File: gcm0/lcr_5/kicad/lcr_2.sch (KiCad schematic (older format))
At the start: 125 parts, among them J1 5V, J2 -5V, J3 Conn_01x01_Male, J7 sin, Q1 BC547, Q2 BC547, Q3 BC547, SW1 1, SW2 2, SW3 SW_DIP_x01, U1 RC4580, U10 RC4580, U11 74HC595, U12 STM32F030F4P6, U13 L7809, U2 74HC4053PW,112, U3 74HC4052PW,118, U4 RC4580, U5 LM2596S-5, U6 LM7805_TO220, U7 RC4580, U8 LM1117-3.3, U9 74HC4053PW,112, Y1 8M

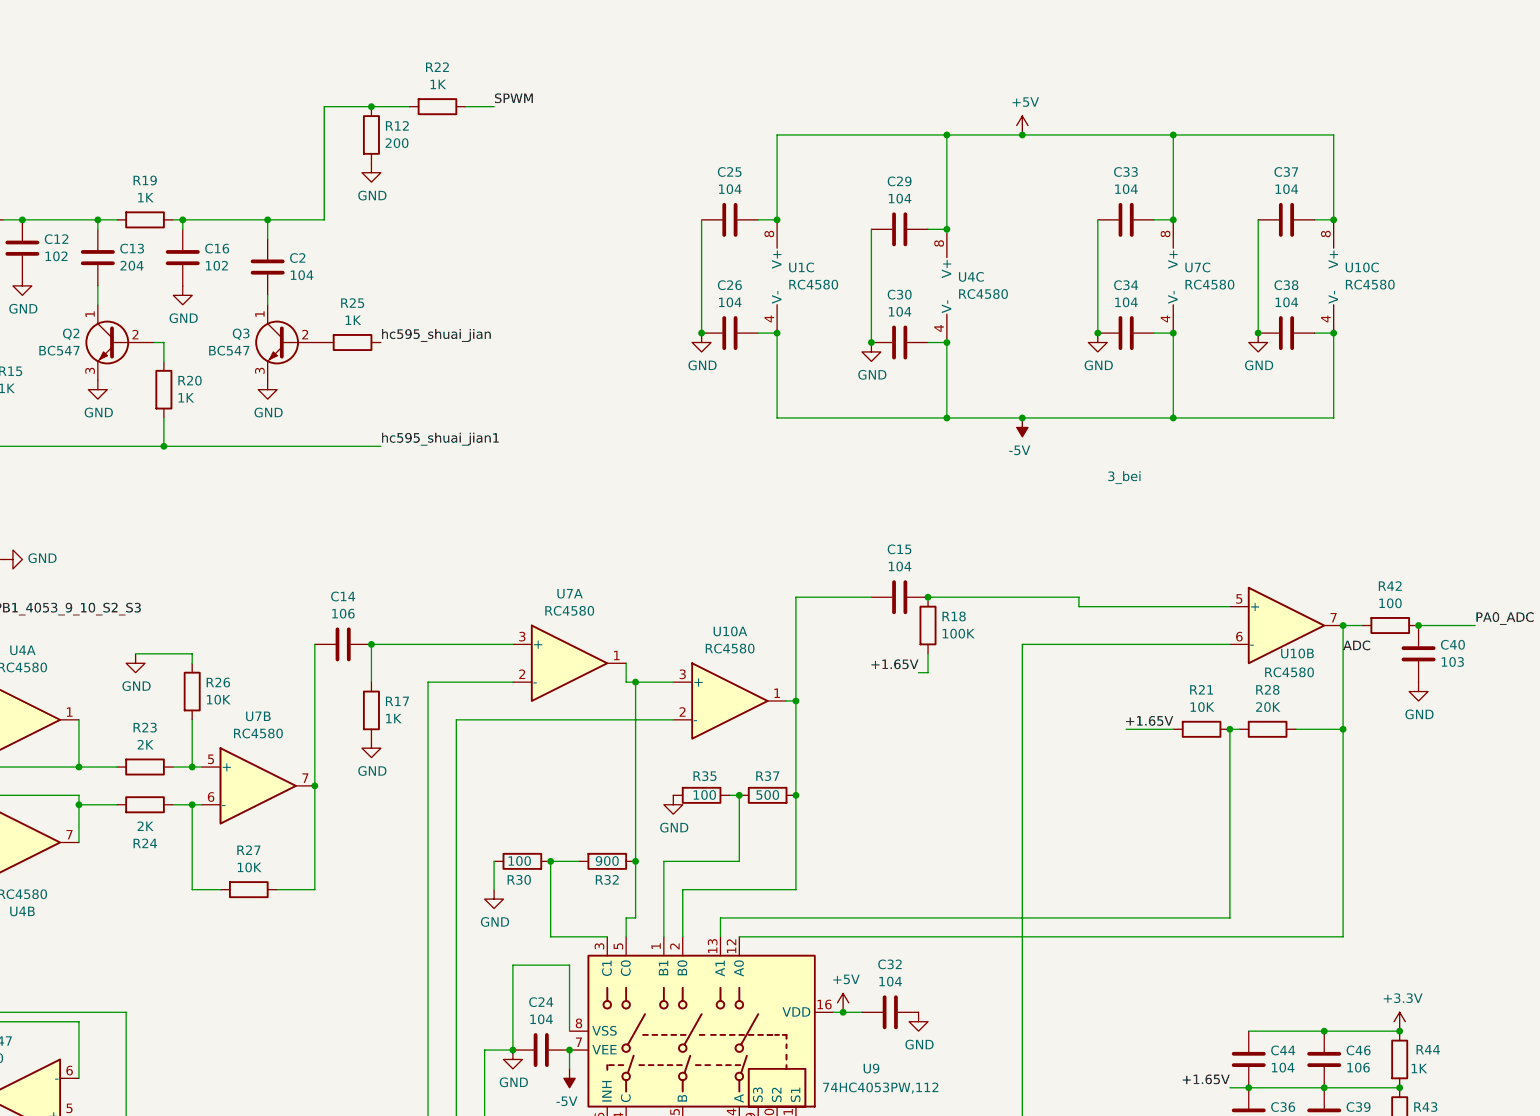
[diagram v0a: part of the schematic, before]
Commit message: 修改采样率
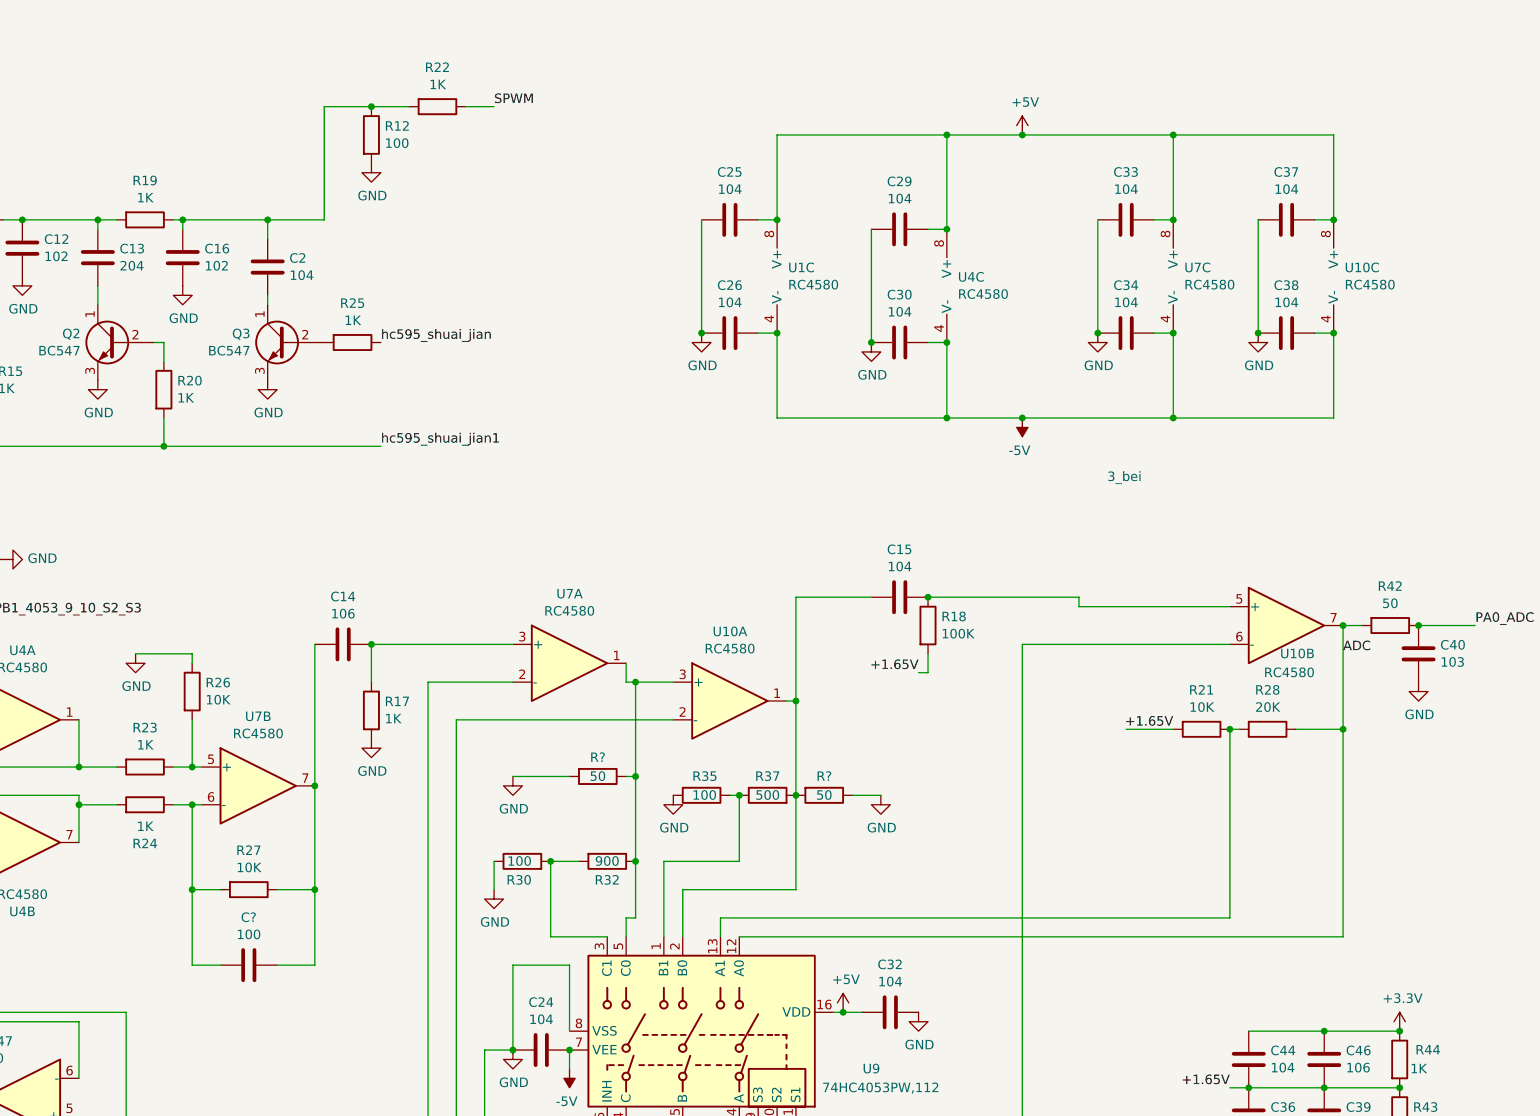
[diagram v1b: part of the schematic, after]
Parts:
- added C?: 100, symbol Device:C
- added R? (x2): 50, symbol Device:R
- R12: value 200 -> 100
- R23, R24: value 2K -> 1K
- R42: value 100 -> 50
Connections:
- net GND: now also R?.1, R?.2
- net at R32.1, U10.3 (+), U7.1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: now also R?.1
- net at R24.1, R27.2, U7.6 (-): now also C?.2
- net at C14.2, R27.1, U7.7: now also C?.1
- net at C15.2, R37.2, U10.1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: now also R?.2
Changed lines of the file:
@@
 P 4350 4450
 F 0 "R23" V 4143 4450 50  0000 C CNN
-F 1 "2K" V 4234 4450 50  0000 C CNN
+F 1 "1K" V 4234 4450 50  0000 C CNN
 F 2 "Resistor_THT:R_Axial_DIN0204_L3.6mm_D1.6mm_P1.90mm_Vertical" V 4280 4450 50  0001 C CNN
 F 3 "~" H 4350 4450 50  0001 C CNN
@@
 P 4350 4650
 F 0 "R24" V 4143 4650 50  0000 C CNN
-F 1 "2K" V 4234 4650 50  0000 C CNN
+F 1 "1K" V 4234 4650 50  0000 C CNN
 F 2 "Resistor_THT:R_Axial_DIN0204_L3.6mm_D1.6mm_P1.90mm_Vertical" V 4280 4650 50  0001 C CNN
 F 3 "~" H 4350 4650 50  0001 C CNN
@@
 P 10950 3700
 F 0 "R42" V 10743 3700 50  0000 C CNN
-F 1 "100" V 10834 3700 50  0000 C CNN
+F 1 "50" V 10834 3700 50  0000 C CNN
 F 2 "Resistor_THT:R_Axial_DIN0204_L3.6mm_D1.6mm_P1.90mm_Vertical" V 10880 3700 50  0001 C CNN
 F 3 "~" H 10950 3700 50  0001 C CNN
@@
 3_bei
 Wire Wire Line
-	6950 4000 6950 4950
+	6950 4000 6950 4500
 Wire Wire Line
 	6900 5250 6950 5250
@@
 P 5550 1100
 F 0 "R12" H 5620 1146 50  0000 L CNN
-F 1 "200" H 5620 1055 50  0000 L CNN
+F 1 "100" H 5620 1055 50  0000 L CNN
 F 2 "Resistor_THT:R_Axial_DIN0204_L3.6mm_D1.6mm_P1.90mm_Vertical" V 5480 1100 50  0001 C CNN
 F 3 "~" H 5550 1100 50  0001 C CNN
@@
 Connection ~ 10600 5850
 Connection ~ 11000 5850
+$Comp
+L Device:C C?
+U 1 1 62123A2D
+P 4900 5500
+F 0 "C?" V 4648 5500 50  0000 C CNN
+F 1 "100" V 4739 5500 50  0000 C CNN
+F 2 "" H 4938 5350 50  0001 C CNN
+F 3 "~" H 4900 5500 50  0001 C CNN
+	1    4900 5500
+	0    1    1    0
+$EndComp
+Wire Wire Line
+	5050 5500 5250 5500
+Wire Wire Line
+	5250 5500 5250 5100
+Connection ~ 5250 5100
+Wire Wire Line
+	4750 5500 4600 5500
+Wire Wire Line
+	4600 5500 4600 5100
+Connection ~ 4600 5100
+$Comp
+L Device:R R?
+U 1 1 621AA26F
+P 6750 4500
+F 0 "R?" V 6650 4500 50  0000 C CNN
+F 1 "50" V 6750 4500 50  0000 C CNN
+F 2 "" V 6680 4500 50  0001 C CNN
+F 3 "~" H 6750 4500 50  0001 C CNN
+	1    6750 4500
+	0    1    1    0
+$EndComp
+$Comp
+L Device:R R?
+U 1 1 621AC5E2
+P 7950 4600
+F 0 "R?" V 7850 4600 50  0000 C CNN
+F 1 "50" V 7950 4600 50  0000 C CNN
+F 2 "" V 7880 4600 50  0001 C CNN
+F 3 "~" H 7950 4600 50  0001 C CNN
+	1    7950 4600
+	0    1    1    0
+$EndComp
+$Comp
+L power:GND #PWR?
+U 1 1 621AF948
+P 6300 4500
+F 0 "#PWR?" H 6300 4250 50  0001 C CNN
+F 1 "GND" H 6305 4327 50  0000 C CNN
+F 2 "" H 6300 4500 50  0001 C CNN
+F 3 "" H 6300 4500 50  0001 C CNN
+	1    6300 4500
+	1    0    0    -1
+$EndComp
+Wire Wire Line
+	6600 4500 6300 4500
+Wire Wire Line
+	6900 4500 6950 4500
+Connection ~ 6950 4500
+Wire Wire Line
+	6950 4500 6950 4950
+$Comp
+L power:GND #PWR?
+U 1 1 62231EF6
+P 8250 4600
+F 0 "#PWR?" H 8250 4350 50  0001 C CNN
+F 1 "GND" H 8255 4427 50  0000 C CNN
+F 2 "" H 8250 4600 50  0001 C CNN
+F 3 "" H 8250 4600 50  0001 C CNN
+	1    8250 4600
+	1    0    0    -1
+$EndComp
+Wire Wire Line
+	8100 4600 8250 4600
 $EndSCHEMATC

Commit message: 修改自动量程
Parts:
- added D11, D12, D13, D14: 1N4007, Diode_THT:D_DO-41_SOD81_P10.16mm_Horizontal, symbol Diode:1N4007
- added R29, R31: 20K, symbol Device:R
- C10: value 204 -> 504
- C2: value 104 -> 404
- C47: value 10 -> 15
- R1: value 50 -> 100
- R23, R24: value 1K -> 200
- R33, R34: renamed from R?; value 50 -> 100
- R5, R6: value 100 -> 20K; footprint Resistor_SMD:R_0805_2012Metric_Pad1.20x1.40mm_HandSolder -> (none)
- gave numbers to parts that had none: 1
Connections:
- net GND: now also D11.2 (A), D12.1 (K), D13.2 (A), D14.1 (K)
- net HC: no longer R5.1
- net HP: now also R6.2, D11.1 (K), D12.2 (A); no longer R5.2, U2.2 (B0)
- net LC: now also R29.2; no longer R6.2, U2.3 (C1)
- net LP: now also R5.2, D13.1 (K), D14.2 (A); no longer R6.1, U2.5 (C0)
- net at U3.13 (X): now also R31.2; no longer U2.1 (B1)
- new net: R31.1, U2.1 (B1)
- new net: R6.1, U2.2 (B0)
- new net: R29.1, U2.3 (C1)
- new net: R5.1, U2.5 (C0)
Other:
- moved on the sheet: R11
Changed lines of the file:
@@
 P 3200 1800
 F 0 "C10" H 3315 1846 50  0000 L CNN
-F 1 "204" H 3315 1755 50  0000 L CNN
+F 1 "504" H 3315 1755 50  0000 L CNN
 F 2 "Capacitor_SMD:C_0603_1608Metric_Pad1.08x0.95mm_HandSolder" H 3238 1650 50  0001 C CNN
 F 3 "~" H 3200 1800 50  0001 C CNN
@@
 Connection ~ 800  6200
 $Comp
-L Device:R R6
-U 1 1 61D537D3
-P 1300 4550
-F 0 "R6" H 1370 4596 50  0000 L CNN
-F 1 "100" H 1370 4505 50  0000 L CNN
-F 2 "Resistor_SMD:R_0805_2012Metric_Pad1.20x1.40mm_HandSolder" V 1230 4550 50  0001 C CNN
-F 3 "~" H 1300 4550 50  0001 C CNN
-	1    1300 4550
-	1    0    0    -1
-$EndComp
-$Comp
 L Device:R R11
 U 1 1 61D7187F
-P 2000 5400
-F 0 "R11" V 1793 5400 50  0000 C CNN
-F 1 "100" V 1884 5400 50  0000 C CNN
-F 2 "Resistor_THT:R_Axial_DIN0204_L3.6mm_D1.6mm_P1.90mm_Vertical" V 1930 5400 50  0001 C CNN
-F 3 "~" H 2000 5400 50  0001 C CNN
-	1    2000 5400
+P 2200 5400
+F 0 "R11" V 1993 5400 50  0000 C CNN
+F 1 "100" V 2084 5400 50  0000 C CNN
+F 2 "Resistor_THT:R_Axial_DIN0204_L3.6mm_D1.6mm_P1.90mm_Vertical" V 2130 5400 50  0001 C CNN
+F 3 "~" H 2200 5400 50  0001 C CNN
+	1    2200 5400
 	0    1    1    0
 $EndComp
@@
 Wire Wire Line
 	3200 5700 3050 5700
-Wire Wire Line
-	2050 4500 1550 4500
-Wire Wire Line
-	1550 4500 1550 4400
-Wire Wire Line
-	1550 4400 1300 4400
-Wire Wire Line
-	2050 4600 1550 4600
-Wire Wire Line
-	1550 4600 1550 4700
-Wire Wire Line
-	1300 4700 1550 4700
 $Comp
 L power:GND #PWR017
@@
 P 4350 4450
 F 0 "R23" V 4143 4450 50  0000 C CNN
-F 1 "1K" V 4234 4450 50  0000 C CNN
+F 1 "200" V 4234 4450 50  0000 C CNN
 F 2 "Resistor_THT:R_Axial_DIN0204_L3.6mm_D1.6mm_P1.90mm_Vertical" V 4280 4450 50  0001 C CNN
 F 3 "~" H 4350 4450 50  0001 C CNN
@@
 P 4350 4650
 F 0 "R24" V 4143 4650 50  0000 C CNN
-F 1 "1K" V 4234 4650 50  0000 C CNN
+F 1 "200" V 4234 4650 50  0000 C CNN
 F 2 "Resistor_THT:R_Axial_DIN0204_L3.6mm_D1.6mm_P1.90mm_Vertical" V 4280 4650 50  0001 C CNN
 F 3 "~" H 4350 4650 50  0001 C CNN
@@
 Wire Wire Line
 	1250 3300 1250 3400
-Connection ~ 1300 4400
-Connection ~ 1300 4700
 Wire Wire Line
 	4450 2750 5600 2750
@@
 P 800 2350
 F 0 "R1" H 870 2396 50  0000 L CNN
-F 1 "50" H 870 2305 50  0000 L CNN
+F 1 "100" H 870 2305 50  0000 L CNN
 F 2 "Resistor_THT:R_Axial_DIN0204_L3.6mm_D1.6mm_P1.90mm_Vertical" V 730 2350 50  0001 C CNN
 F 3 "~" H 800 2350 50  0001 C CNN
@@
 Wire Wire Line
 	1350 5550 1650 5550
-Wire Wire Line
-	1300 4700 1300 5400
 Connection ~ 1300 5550
 Wire Wire Line
 	1300 5550 1350 5550
-Wire Wire Line
-	2150 5400 3300 5400
-Wire Wire Line
-	1850 5400 1300 5400
 Connection ~ 1300 5400
 Wire Wire Line
@@
 Wire Notes Line
 	700  4200 700  4700
-Connection ~ 1050 3000
-Wire Wire Line
-	1050 3000 1250 3000
-Connection ~ 1250 3300
-$Comp
-L Device:R R5
-U 1 1 61D0188C
-P 1250 3150
-F 0 "R5" H 1320 3196 50  0000 L CNN
-F 1 "100" H 1320 3105 50  0000 L CNN
-F 2 "Resistor_SMD:R_0805_2012Metric_Pad1.20x1.40mm_HandSolder" V 1180 3150 50  0001 C CNN
-F 3 "~" H 1250 3150 50  0001 C CNN
-	1    1250 3150
-	1    0    0    -1
-$EndComp
 $Comp
 L Amplifier_Operational:RC4580 U7
@@
 P 5000 1800
 F 0 "C2" H 5115 1846 50  0000 L CNN
-F 1 "104" H 5115 1755 50  0000 L CNN
+F 1 "404" H 5115 1755 50  0000 L CNN
 F 2 "Capacitor_SMD:C_0603_1608Metric_Pad1.08x0.95mm_HandSolder" H 5038 1650 50  0001 C CNN
 F 3 "~" H 5000 1800 50  0001 C CNN
@@
 P 3400 5950
 F 0 "C47" H 3515 5996 50  0000 L CNN
-F 1 "10" H 3515 5905 50  0000 L CNN
+F 1 "15" H 3515 5905 50  0000 L CNN
 F 2 "Capacitor_SMD:C_0603_1608Metric_Pad1.08x0.95mm_HandSolder" H 3438 5800 50  0001 C CNN
 F 3 "~" H 3400 5950 50  0001 C CNN
@@
 Connection ~ 6950 4000
 Wire Wire Line
-	1850 4200 1850 3300
-Wire Wire Line
-	1850 4200 2050 4200
-Wire Wire Line
 	2350 5050 2000 5050
 Wire Wire Line
@@
 Wire Wire Line
 	3050 3800 3500 3800
-Wire Wire Line
-	2000 4300 2000 5050
-Wire Wire Line
-	1250 3300 1850 3300
 Connection ~ 10700 3700
 $Comp
@@
 Connection ~ 11000 5850
 $Comp
-L Device:C C?
+L Device:C C23
 U 1 1 62123A2D
 P 4900 5500
-F 0 "C?" V 4648 5500 50  0000 C CNN
+F 0 "C23" V 4648 5500 50  0000 C CNN
 F 1 "100" V 4739 5500 50  0000 C CNN
 F 2 "" H 4938 5350 50  0001 C CNN
@@
 Connection ~ 4600 5100
 $Comp
-L Device:R R?
+L Device:R R33
 U 1 1 621AA26F
 P 6750 4500
-F 0 "R?" V 6650 4500 50  0000 C CNN
-F 1 "50" V 6750 4500 50  0000 C CNN
+F 0 "R33" V 6650 4500 50  0000 C CNN
+F 1 "100" V 6750 4500 50  0000 C CNN
 F 2 "" V 6680 4500 50  0001 C CNN
 F 3 "~" H 6750 4500 50  0001 C CNN
@@
 $EndComp
 $Comp
-L Device:R R?
+L Device:R R34
 U 1 1 621AC5E2
 P 7950 4600
-F 0 "R?" V 7850 4600 50  0000 C CNN
-F 1 "50" V 7950 4600 50  0000 C CNN
+F 0 "R34" V 7850 4600 50  0000 C CNN
+F 1 "100" V 7950 4600 50  0000 C CNN
 F 2 "" V 7880 4600 50  0001 C CNN
 F 3 "~" H 7950 4600 50  0001 C CNN
@@
 $EndComp
 $Comp
-L power:GND #PWR?
+L power:GND #PWR044
 U 1 1 621AF948
 P 6300 4500
-F 0 "#PWR?" H 6300 4250 50  0001 C CNN
+F 0 "#PWR044" H 6300 4250 50  0001 C CNN
 F 1 "GND" H 6305 4327 50  0000 C CNN
 F 2 "" H 6300 4500 50  0001 C CNN
@@
 	6950 4500 6950 4950
 $Comp
-L power:GND #PWR?
+L power:GND #PWR048
 U 1 1 62231EF6
 P 8250 4600
-F 0 "#PWR?" H 8250 4350 50  0001 C CNN
+F 0 "#PWR048" H 8250 4350 50  0001 C CNN
 F 1 "GND" H 8255 4427 50  0000 C CNN
 F 2 "" H 8250 4600 50  0001 C CNN
@@
 Wire Wire Line
 	8100 4600 8250 4600
+$Comp
+L Device:R R6
+U 1 1 622DB700
+P 1800 3300
+F 0 "R6" V 1593 3300 50  0000 C CNN
+F 1 "20K" V 1684 3300 50  0000 C CNN
+F 2 "" V 1730 3300 50  0001 C CNN
+F 3 "~" H 1800 3300 50  0001 C CNN
+	1    1800 3300
+	0    1    1    0
+$EndComp
+$Comp
+L Device:R R5
+U 1 1 622DD89B
+P 1750 4400
+F 0 "R5" V 1543 4400 50  0000 C CNN
+F 1 "20K" V 1634 4400 50  0000 C CNN
+F 2 "" V 1680 4400 50  0001 C CNN
+F 3 "~" H 1750 4400 50  0001 C CNN
+	1    1750 4400
+	0    1    1    0
+$EndComp
+Wire Wire Line
+	1650 3300 1250 3300
+Connection ~ 1250 3300
+Wire Wire Line
+	1950 3300 1950 4200
+Wire Wire Line
+	1950 4200 2050 4200
+Wire Wire Line
+	1900 4400 1900 4500
+Wire Wire Line
+	1900 4500 2050 4500
+Wire Wire Line
+	1600 4400 1400 4400
+Connection ~ 1300 4400
+Wire Wire Line
+	1900 4600 2050 4600
+$Comp
+L Diode:1N4007 D11
+U 1 1 624E92F8
+P 1400 2850
+F 0 "D11" H 1400 3067 50  0000 C CNN
+F 1 "1N4007" H 1400 2976 50  0000 C CNN
+F 2 "Diode_THT:D_DO-41_SOD81_P10.16mm_Horizontal" H 1400 2675 50  0001 C CNN
+F 3 "http://www.vishay.com/docs/88503/1n4001.pdf" H 1400 2850 50  0001 C CNN
+	1    1400 2850
+	1    0    0    -1
+$EndComp
+$Comp
+L Diode:1N4007 D12
+U 1 1 624EBBB9
+P 1400 3000
+F 0 "D12" H 1400 3200 50  0000 C CNN
+F 1 "1N4007" H 1400 3100 50  0000 C CNN
+F 2 "Diode_THT:D_DO-41_SOD81_P10.16mm_Horizontal" H 1400 2825 50  0001 C CNN
+F 3 "http://www.vishay.com/docs/88503/1n4001.pdf" H 1400 3000 50  0001 C CNN
+	1    1400 3000
+	-1   0    0    1
+$EndComp
+Wire Wire Line
+	1250 2850 1250 3000
+Connection ~ 1250 3000
+Wire Wire Line
+	1250 3000 1250 3300
+$Comp
+L power:GND #PWR042
+U 1 1 62578CEA
+P 2100 2850
+F 0 "#PWR042" H 2100 2600 50  0001 C CNN
+F 1 "GND" H 2105 2677 50  0000 C CNN
+F 2 "" H 2100 2850 50  0001 C CNN
+F 3 "" H 2100 2850 50  0001 C CNN
+	1    2100 2850
+	1    0    0    -1
+$EndComp
+Wire Wire Line
+	1550 3000 1550 2850
+Wire Wire Line
+	1550 2850 2100 2850
+Connection ~ 1550 2850
+Wire Wire Line
+	1300 4700 1300 5400
+$Comp
+L Diode:1N4007 D13
+U 1 1 626C7C25
+P 1550 4700
+F 0 "D13" H 1550 4917 50  0000 C CNN
+F 1 "1N4007" H 1550 4826 50  0000 C CNN
+F 2 "Diode_THT:D_DO-41_SOD81_P10.16mm_Horizontal" H 1550 4525 50  0001 C CNN
+F 3 "http://www.vishay.com/docs/88503/1n4001.pdf" H 1550 4700 50  0001 C CNN
+	1    1550 4700
+	1    0    0    -1
+$EndComp
+$Comp
+L Diode:1N4007 D14
+U 1 1 626C93AB
+P 1550 4850
+F 0 "D14" H 1550 5050 50  0000 C CNN
+F 1 "1N4007" H 1550 4950 50  0000 C CNN
+F 2 "Diode_THT:D_DO-41_SOD81_P10.16mm_Horizontal" H 1550 4675 50  0001 C CNN
+F 3 "http://www.vishay.com/docs/88503/1n4001.pdf" H 1550 4850 50  0001 C CNN
+	1    1550 4850
+	-1   0    0    1
+$EndComp
+$Comp
+L Device:R R29
+U 1 1 62753D7F
+P 1850 5250
+F 0 "R29" H 1920 5296 50  0000 L CNN
+F 1 "20K" H 1920 5205 50  0000 L CNN
+F 2 "" V 1780 5250 50  0001 C CNN
+F 3 "~" H 1850 5250 50  0001 C CNN
+	1    1850 5250
+	1    0    0    -1
+$EndComp
+Wire Wire Line
+	1300 5400 1850 5400
+Wire Wire Line
+	2350 5400 3300 5400
+Connection ~ 1850 5400
+Wire Wire Line
+	1850 5400 2050 5400
+Wire Wire Line
+	1850 5100 1900 5100
+Wire Wire Line
+	1900 4600 1900 5100
+Wire Wire Line
+	1400 4850 1400 4700
+Connection ~ 1400 4400
+Wire Wire Line
+	1400 4400 1300 4400
+Connection ~ 1400 4700
+Wire Wire Line
+	1400 4700 1400 4400
+$Comp
+L power:GND #PWR039
+U 1 1 629AA0F3
+P 1800 4750
+F 0 "#PWR039" H 1800 4500 50  0001 C CNN
+F 1 "GND" H 1805 4577 50  0000 C CNN
+F 2 "" H 1800 4750 50  0001 C CNN
+F 3 "" H 1800 4750 50  0001 C CNN
+	1    1800 4750
+	1    0    0    -1
+$EndComp
+Wire Wire Line
+	1700 4700 1700 4750
+Wire Wire Line
+	1800 4750 1700 4750
+Connection ~ 1700 4750
+Wire Wire Line
+	1700 4750 1700 4850
+$Comp
+L Device:R R31
+U 1 1 62A7BF50
+P 2000 4900
+F 0 "R31" H 2070 4946 50  0000 L CNN
+F 1 "20K" H 2070 4855 50  0000 L CNN
+F 2 "" V 1930 4900 50  0001 C CNN
+F 3 "~" H 2000 4900 50  0001 C CNN
+	1    2000 4900
+	1    0    0    -1
+$EndComp
+Wire Wire Line
+	2000 4750 2000 4300
 $EndSCHEMATC

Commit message: 修改电路
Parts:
- added C28: 103, symbol Device:C
- added C48: 104, symbol Device:C
- added C49, C50: 470uF, symbol Device:CP
- added R36, R55: 1K, symbol Device:R
- added R38: 900, symbol Device:R
- added R39, R40, R56, R57: 100, symbol Device:R
- added R41: 500, symbol Device:R
- added R53: 100K, symbol Device:R
- added R54: 2K, symbol Device:R
- C14: value 106 -> 104
- C23: value 100 -> 103
- R21, R26, R27: value 10K -> 1K
- R23, R24: value 200 -> 1K
- R28: value 20K -> 2K
- R34: value 100 -> 1K
- U1, U10, U4, U7: value RC4580 -> MC4580G-S08-R
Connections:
- net +5V: now also C49.1
- net -5V: now also C50.1
- net ADC: no longer U9.12 (A0)
- net GND: now also C49.2, C50.2, R39.2, R40.2, R53.2, R55.2; no longer R33.2, R34.1
- net HC: now also R56.1
- net HP: now also R56.2
- net LC: now also R57.2
- net LP: now also R57.1
- net at R23.2, U4.1: now also C23.1, R34.1; no longer U4.2 (-)
- net at R24.2, U4.7: now also C28.1, R36.1; no longer U4.6 (-)
- net at U7.2 (-): now also R30.2, R32.2; no longer U9.4 (C)
- net at R24.1, R27.2, U7.6 (-): no longer C23.2
- net at R27.1, U7.7: now also U9.3 (C1), R38.1; no longer C14.2, C23.1
- net at R21.1, R28.2: now also U10.6 (-); no longer U9.13 (A1)
- net at R35.1, R37.1: now also U10.2 (-); no longer U9.1 (B1)
- net at U9.14 (A): now also C15.2; no longer U10.6 (-)
- net at U9.15 (B): now also C48.2; no longer U10.2 (-)
- new net: C23.2, R33.2, R34.2, U4.2 (-)
- new net: C28.2, R33.1, R36.2, U4.6 (-)
- new net: R54.2, R55.1, U9.12 (A0)
- new net: R37.2, R54.1, U10.1, U9.13 (A1)
- new net: C14.2, U9.4 (C)
- new net: R38.2, R39.1, U9.5 (C0)
- new net: C48.1, R53.1, U10.3 (+)
- new net 4053_1: R32.1, R41.1, U7.1, U9.1 (B1)
- new net 4053_2: R40.1, R41.2, U9.2 (B0)
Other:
- moved on the sheet: C11, C14, C15, C24, C32, C36, C39, C40, C44, C46, R17, R18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

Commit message: 修改滤波电路
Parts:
- removed C23, C28: 103, symbol Device:C
- C10: value 504 -> 2uF
- C13: value 204 -> 2uF
- C14, C15, C48: value 104 -> 106
- C2: value 404 -> 204
- R12: value 100 -> 200
- R17, R21, R55: value 1K -> 10K
- R18, R53: value 100K -> 10K
- R28, R54: value 2K -> 20K
- R42: value 50 -> 100
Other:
- moved on the sheet: R23, R24, R26, R27, R33, R34, R36, U4A, U4B, U7B
